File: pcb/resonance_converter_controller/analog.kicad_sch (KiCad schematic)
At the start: 59 parts, among them U10 INA280A1xDCK, U11 INA280A1xDCK, U12 INA280A1xDCK, U17 TL3116, U18 OPA2356xxDGK, U19 OPA2325, U20 OPA356xxDBV, U5 OPA2325, U7 OPA2356xxDGK, U8 OPA356xxDBV, U9 INA280A1xDCK

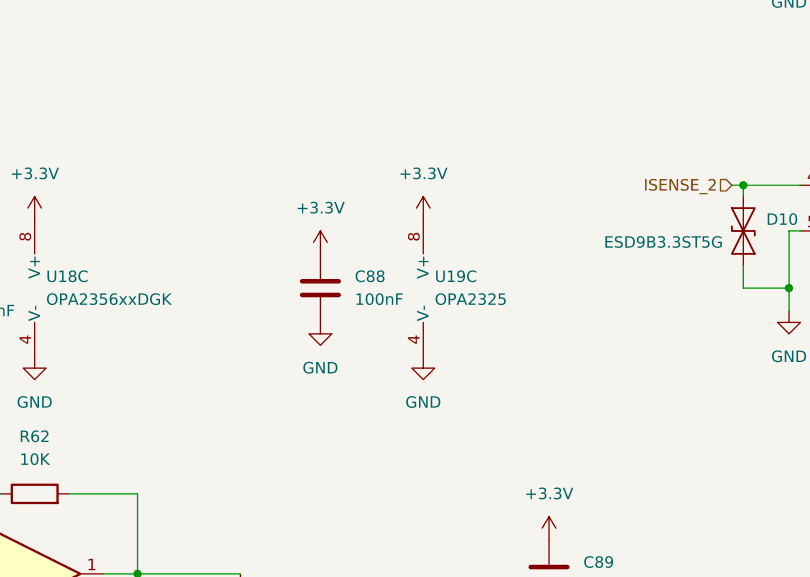
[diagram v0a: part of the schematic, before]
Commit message: First routing without testpoints
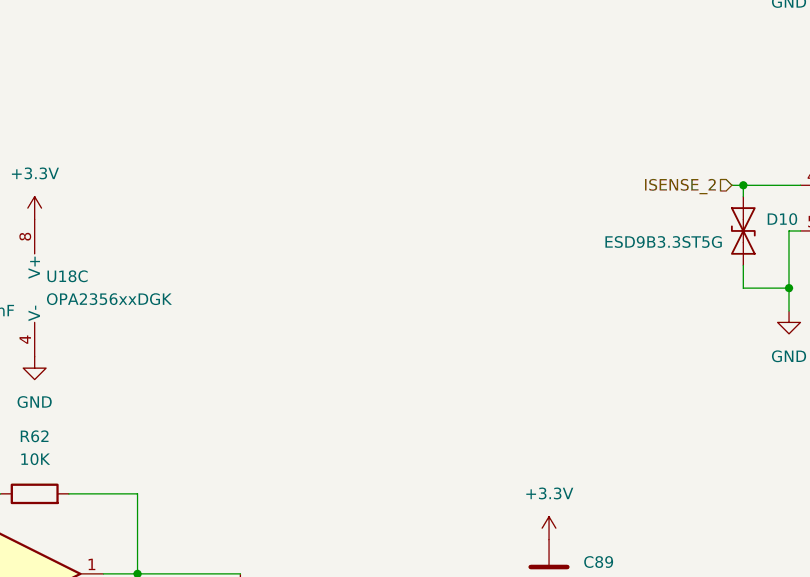
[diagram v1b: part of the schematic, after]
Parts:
- removed C88: 100nF, Capacitor_SMD:C_0402_1005Metric, symbol Device:C
- removed U19: OPA2325, Package_SO:SOIC-8_3.9x4.9mm_P1.27mm, symbol Amplifier_Operational:OPA2325

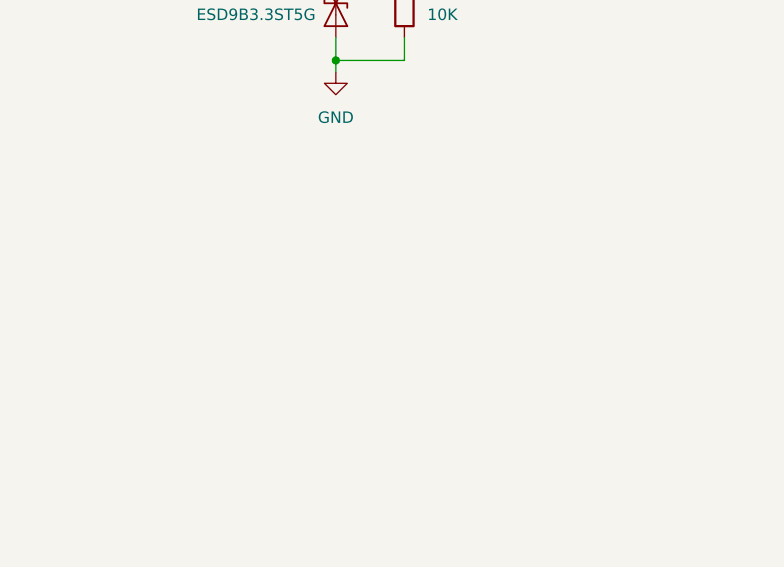
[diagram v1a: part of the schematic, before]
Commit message: Add io panel and fix controller pcb
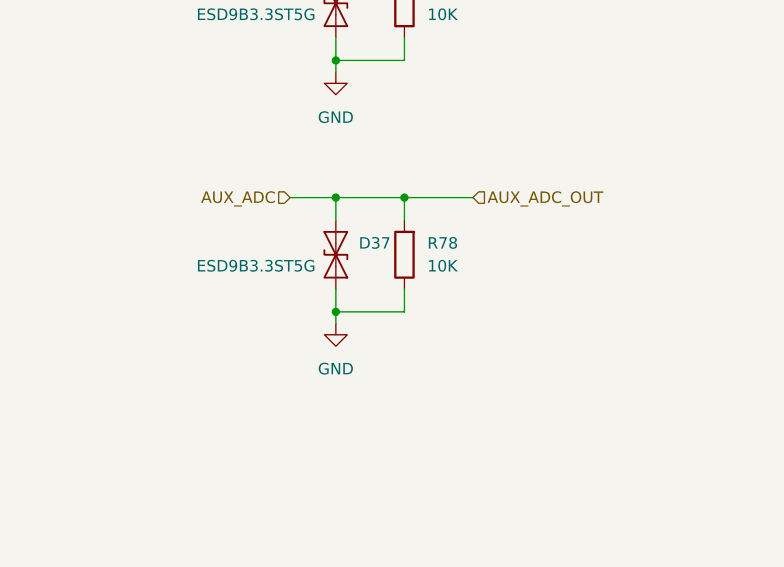
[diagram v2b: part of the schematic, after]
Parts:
- added D37: ESD9B3.3ST5G, Diode_SMD:D_SOD-923, symbol Diode:ESD9B3.3ST5G
- added R78: 10K, Resistor_SMD:R_0402_1005Metric, symbol Device:R
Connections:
- net GND: now also D37.1 (A1), R78.1
- new net AUX_ADC: D37.2 (A2), R78.2

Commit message: Add digital pots to auto adjust gain
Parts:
- removed R36, R65: 10K, Resistor_SMD:R_0402_1005Metric, symbol Device:R
- removed U10, U11, U12, U9: INA280A1xDCK, Package_TO_SOT_SMD:SOT-353_SC-70-5, symbol Amplifier_Current:INA280A1xDCK
- added C103, C104, C97, C98: 100nF, Capacitor_SMD:C_0402_1005Metric, symbol Device:C
- added D35: ESD9B3.3ST5G, Diode_SMD:D_SOD-923, symbol Diode:ESD9B3.3ST5G
- added R76: 10K, Resistor_SMD:R_0402_1005Metric, symbol Device:R
- added U10, U11, U27, U9: INA169, Package_TO_SOT_SMD:SOT-23-5, symbol Amplifier_Current:INA169
- added U12, U24: MCP4441-xxxx-ST, Package_DFN_QFN:Texas_RGP0020H_VQFN-20-1EP_4x4mm_P0.5mm_EP2.4x2.4mm_ThermalVias, symbol Potentiometer_Digital:MCP4441-xxxx-ST
- added U23, U28: OPA356xxDBV, Package_TO_SOT_SMD:SOT-23-5, symbol Amplifier_Operational:OPA356xxDBV
- U18, U5, U7: footprint Package_SO:SOIC-8_3.9x4.9mm_P1.27mm -> Package_SO:VSSOP-8_3x3mm_P0.65mm
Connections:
- net +3.3V: now also U10.5 (V+), U11.5 (V+), U27.5 (V+), U9.5 (V+)
- net GND: now also C103.2, C104.2, C97.2, C98.2, D35.2 (A2), U10.2 (GND), U10.4 (-), U11.2 (GND), U11.4 (-), U12.12 (P0W), U12.13 (P0B), U12.18 (P2B), U12.19 (P2W), U12.2 (P3W), U12.3 (P3B), U12.7 (VSS), U12.8 (P1B), U12.9 (P1W), U23.2 (V-), U24.12 (P0W), U24.13 (P0B), U24.18 (P2B), U24.19 (P2W), U24.2 (P3W), U24.3 (P3B), U24.4 (HVC/A0), U24.7 (VSS), U27.2 (GND), U27.4 (-), U28.2 (V-), U9.2 (GND), U9.4 (-)
- net ISENSE_1: now also U9.3 (+)
- net ISENSE_1_OUT: now also U12.20 (P2A), U9.1
- net ISENSE_2: now also U27.3 (+)
- net ISENSE_2_OUT: now also U12.1 (P3A), U27.1
- net ISENSE_3: now also U10.3 (+)
- net ISENSE_3_OUT: now also U10.1, U12.10 (P1A)
- net ISENSE_4: now also U11.3 (+)
- net ISENSE_4_OUT: now also U11.1, U12.11 (P0A)
- net VSENSE_IN: now also U28.3 (+)
- net at R37.1, U8.4 (-): now also U24.1 (P3A)
- net at R66.1, U20.4 (-): now also U24.20 (P2A)
- new net: R76.1, U24.11 (P0A), U28.4 (-)
- new net: U23.1, U23.4 (-), U24.10 (P1A)
- new net DAC_IN: U23.3 (+)
- new net DAC_OUT: D35.1 (A1), U24.8 (P1B), U24.9 (P1W)
- new net SCL: U12.5 (SCL), U24.5 (SCL)
- new net SDA: U12.6 (SDA), U24.6 (SDA)
- new net VAA: C97.1, C98.1, U23.5 (V+), U28.5 (V+)
- new net VCC: C103.1, C104.1, U12.15 (~{RESET}), U12.16 (A1), U12.17 (VDD), U12.4 (HVC/A0), U24.15 (~{RESET}), U24.16 (A1), U24.17 (VDD)
- new net VSENSE_OUT: R76.2, U28.1
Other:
- moved on the sheet: C65, C66, C67, D13, D37, D9, R31, R32, R33, R34, R35, R37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
